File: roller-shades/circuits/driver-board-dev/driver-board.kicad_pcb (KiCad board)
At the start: 2 copper layers, 41 x 47 mm, 22 parts, among them J1 NEMA17_Conn, J2 DS18B20_Conn, J3 Power_Conn, J4 Window_Conn, J5 A3144_Conn, U1 AMS1117-5.0, U2 AS5601-ASOM, U4 WeMos_D1_mini

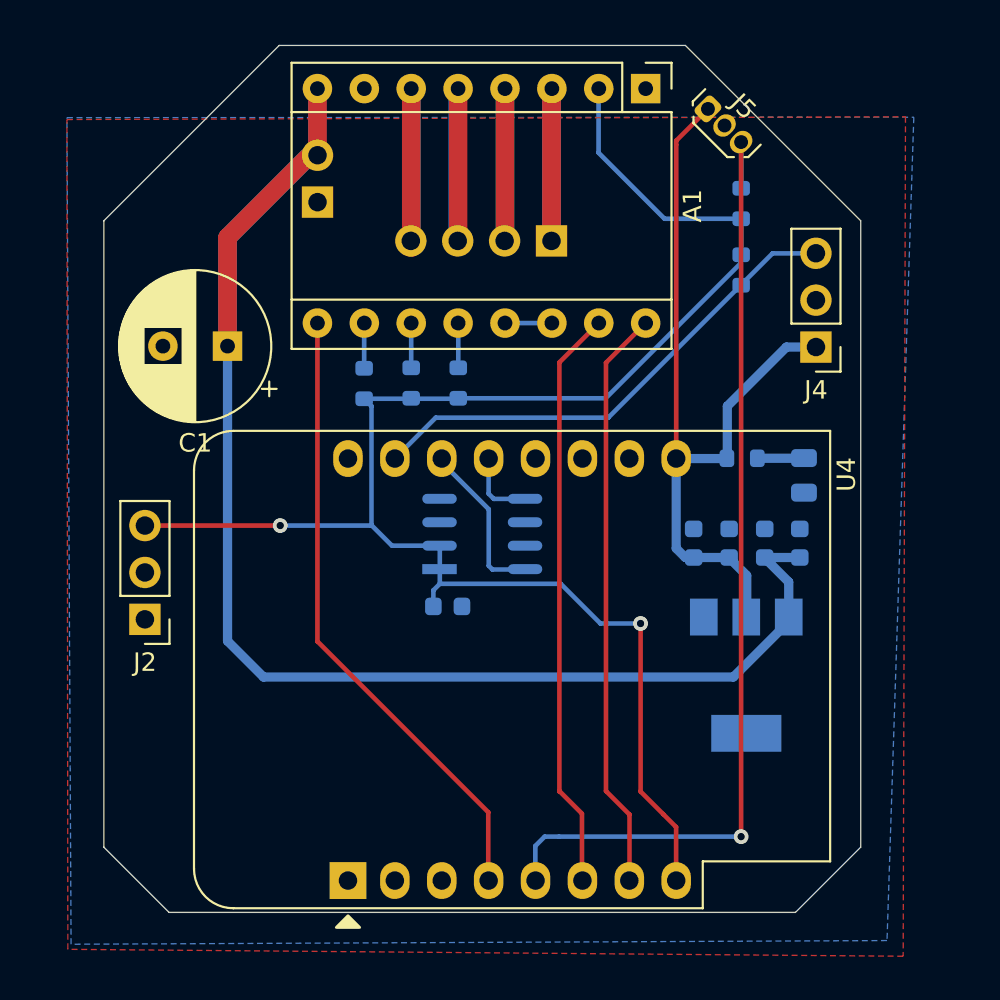
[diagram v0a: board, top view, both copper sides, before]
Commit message: Refractored dependencies into each project and added missing folders
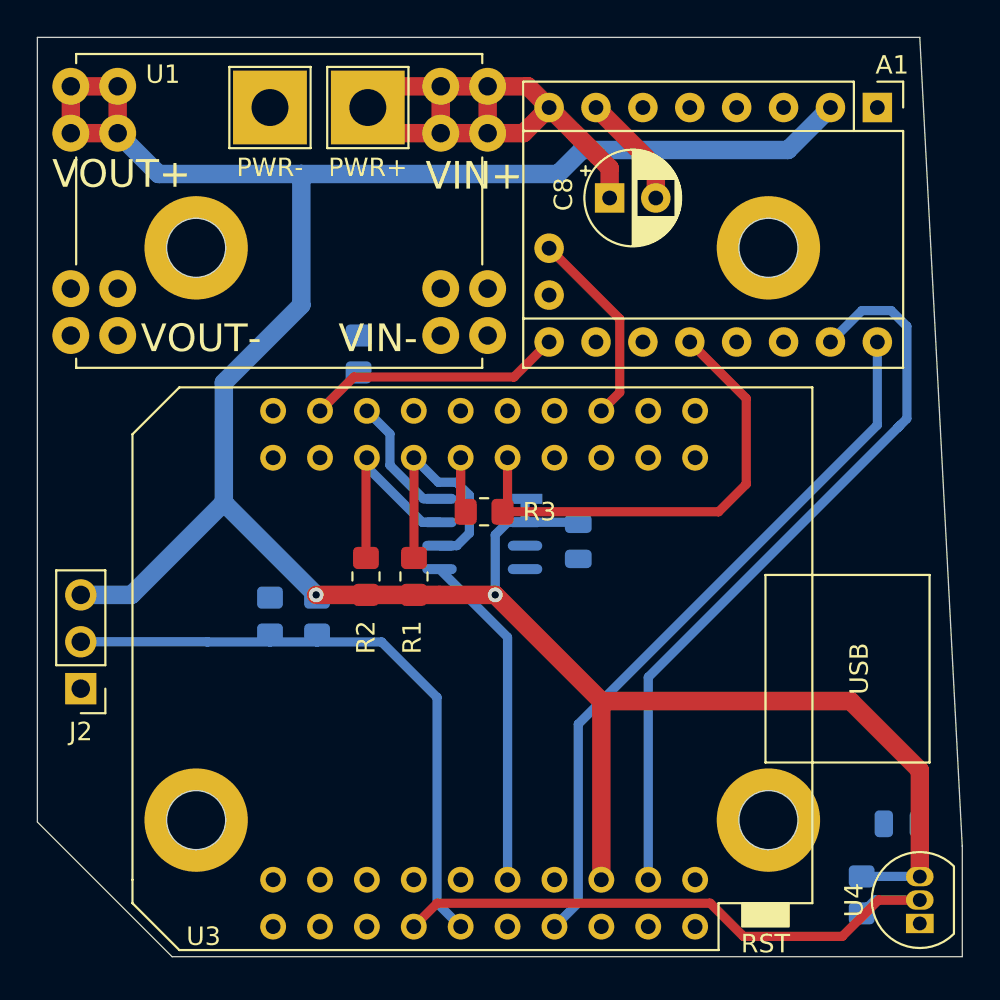
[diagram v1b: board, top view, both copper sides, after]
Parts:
- removed C3, C6: 10µF, Capacitor_SMD:C_0603_1608Metric
- removed C4, C7: 100nF, Capacitor_SMD:C_0603_1608Metric
- removed D1: DIODE, Diode_SMD:D_0805_2012Metric
- removed J1: NEMA17_Conn, Connector_PinHeader_2.54mm:PinHeader_1x04_P2.54mm_Horizontal
- removed J3: Power_Conn, Connector_PinHeader_2.54mm:PinHeader_1x02_P2.54mm_Vertical
- removed J4: Window_Conn, Connector_PinHeader_2.54mm:PinHeader_1x03_P2.54mm_Vertical
- removed J5: A3144_Conn, Package_TO_SOT_THT:TO-92Flat
- added C8: 100µF, Capacitor_THT:CP_Radial_D5.0mm_P2.50mm, F.Cu at (67.7, 34.1)
- added H1: MountingHole, MountingHole:MountingHole_3.2mm_M3_DIN965_Pad, F.Cu at (45.3, 36.8)
- added H2: MountingHole, MountingHole:MountingHole_3.2mm_M3_DIN965_Pad, F.Cu at (76.3, 67.8)
- added H3: MountingHole, MountingHole:MountingHole_3.2mm_M3_DIN965_Pad, F.Cu at (76.3, 36.8)
- added H4: MountingHole, MountingHole:MountingHole_3.2mm_M3_DIN965_Pad, F.Cu at (45.3, 67.8)
- added PWR+: Conn_01x01_Female, TestPoint:TestPoint_THTPad_4.0x4.0mm_Drill2.0mm, F.Cu at (54.6, 29.2)
- added PWR-: Conn_01x01_Female, TestPoint:TestPoint_THTPad_4.0x4.0mm_Drill2.0mm, F.Cu at (49.3, 29.2)
- added R6: 10K, Resistor_SMD:R_0805_2012Metric_Pad1.20x1.40mm_HandSolder, B.Cu at (81.4, 71.9)
- added U3: mini_esp32, SHP_Deps:Wemos_D1_mini32, F.Cu at (60.9, 59.6)
- A1: value Pololu_Breakout_A4988 -> BigTreeTech_TMC2209_V12; footprint Module:Pololu_Breakout-16_15.2x20.3mm -> SHP_Deps:BigTreeTech_TMC22xx_Breakout-16_15.2x20.3mm
- C1: value 100µF -> 100nF; footprint Capacitor_THT:CP_Radial_D8.0mm_P3.50mm -> Capacitor_SMD:C_0805_2012Metric; moved to B.Cu
- C2: footprint Capacitor_SMD:C_0603_1608Metric -> Capacitor_SMD:C_0805_2012Metric
- J2: value DS18B20_Conn -> AUX1
- R1, R2: value 10k -> 10K; footprint Resistor_SMD:R_0603_1608Metric -> Resistor_SMD:R_0805_2012Metric_Pad1.20x1.40mm_HandSolder; moved to F.Cu
- R3: value 10k -> 1k; footprint Resistor_SMD:R_0603_1608Metric -> Resistor_SMD:R_0805_2012Metric_Pad1.20x1.40mm_HandSolder; moved to F.Cu
- R4, R5: value 10k -> 1k; footprint Resistor_SMD:R_0603_1608Metric -> Resistor_SMD:R_0805_2012Metric_Pad1.20x1.40mm_HandSolder
- R7: value 1K -> 10K; footprint Resistor_SMD:R_0603_1608Metric -> Resistor_SMD:R_0805_2012Metric_Pad1.20x1.40mm_HandSolder
- U1: value AMS1117-5.0 -> DM0x-DC-DC; footprint Package_TO_SOT_SMD:SOT-223-3_TabPin2 -> SHP_Deps:DM02-DC-DC; moved to F.Cu
- U4: value WeMos_D1_mini -> DS18S20; footprint Module:WEMOS_D1_mini_light -> Package_TO_SOT_THT:TO-92_Inline
- moved C1 44.7 mm to (83.5, 68.0)
- moved U1 35.7 mm to (49.8, 34.8), turned to 0 degrees
- moved R5 33.9 mm to (49.3, 56.8)
- moved U4 31.1 mm to (84.5, 73.4)
- moved R4 29.7 mm to (51.9, 56.8), turned to 90 degrees
- moved R7 21.5 mm to (54.1, 42.6), turned to 270 degrees
- moved A1 12.6 mm to (82.2, 29.2)
- moved R1 10.8 mm to (57.1, 54.6)
- moved R2 10.8 mm to (54.5, 54.6)
- moved C2 7.90 mm to (66.0, 52.7), turned to 270 degrees
- moved R3 7.11 mm to (60.9, 51.1), turned to 180 degrees
- moved J2 5.12 mm to (39.1, 60.7)
- turned U2 to 180 degrees
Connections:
- A1 pad 10: /STPR_MS1 -> Net-(A1-Pad10)
- A1 pad 11: /STPR_MS2 -> Net-(A1-Pad11)
- A1 pad 12: /STPR_MS3 -> /TMC2209_PDN
- A1 pad 14: Net-(A1-Pad13) -> Net-(A1-Pad14)
- A1 pad 15: /STPR_STP -> /TMC2209_STEP
- A1 pad 16: /STPR_DIR -> /TMC2209_DIR
- A1 pad 8: VDD -> VBUS
- A1 pad 9: /STPR_ENA -> /TMC2209_EN
- C1 pad 1: VDD -> +3V3
- J2 pad 2: /GPIO12 -> /CONN_AUX1
- R1 pad 2: /STPR_MS1 -> /I2C_SDA
- R2 pad 2: /STPR_MS2 -> /I2C_SCL
- R3 pad 1: +3V3 -> /TMC2209_PDN
- R3 pad 2: /STPR_MS3 -> Net-(R3-Pad2)
- R4 pad 1: +3V3 -> /CONN_AUX1
- R4 pad 2: /WINDOW_SIG -> +3V3
- R5 pad 1: +3V3 -> /CONN_AUX1
- R5 pad 2: /ROLLER_SIG -> GND
- R7 pad 1: Net-(D1-Pad1) -> GND
- R7 pad 2: +5V -> /TMC2209_EN
- U1 pad 2: +5V -> VBUS
- U1 pad 3: VDD -> +3V3
- U2 pad 5: /ENC_A -> /AS5601_ABI_B
- U2 pad 6: Net-(U2-Pad6) -> /I2C_SDA
- U2 pad 7: Net-(U2-Pad7) -> /I2C_SCL
- U2 pad 8: /ENC_B -> /AS5601_ABI_A
- U4 pad 1: Net-(U4-Pad1) -> GND
- U4 pad 2: Net-(U4-Pad2) -> /TEMP_SENSOR
- U4 pad 3: Net-(U4-Pad3) -> +3V3
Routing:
- net VDD: track 86.1 -> 0.00 mm
- net +3V3: track 91.9 -> 154.6 mm
- net /ROLLER_SIG: track 53.3 -> 0.00 mm, vias 1 -> 0
- net +5V: track 43.3 -> 0.00 mm
- net /TMC2209_STEP: track 0.00 -> 41.2 mm
- net /TMC2209_DIR: track 0.00 -> 38.9 mm
- net VBUS: track 0.00 -> 34.9 mm
- net /CONN_AUX1: track 0.00 -> 34.3 mm
- net /STPR_ENA: track 34.0 -> 0.00 mm
- net /TEMP_SENSOR: track 0.00 -> 32.9 mm
- net /STPR_DIR: track 31.6 -> 0.00 mm
- net /STPR_STP: track 31.6 -> 0.00 mm
- net /WINDOW_SIG: track 27.4 -> 0.00 mm
- net /TMC2209_PDN: track 0.00 -> 25.8 mm
- net /AS5601_ABI_B: track 0.00 -> 18.4 mm
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- removed copper zone on B.Cu, net GND
- removed copper zone on F.Cu, net GND
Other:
- board size 41 x 47 mm -> 50.1 x 49.8 mm
- board text removed: "www.github.com/slimcdk/ smart-home-projects.git"
